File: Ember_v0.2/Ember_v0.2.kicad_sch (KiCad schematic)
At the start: 87 parts, among them J3 DROGUE, J4 BATT_CONN, J5 MAIN, J6 MAN2, J7 DROGUE2, J8 ARM, Q1 SISA96DN-T1, Q2 SISA96DN-T1, Q3 SISA96DN-T1, Q4 SISA96DN-T1, Q5 CJ3400, U1 LDO Regulator 5v, U2 BNO055, U4 BMP280, U6 ADS1220xPW, U7 RPi Pico 2, U8 ADS1220xPW

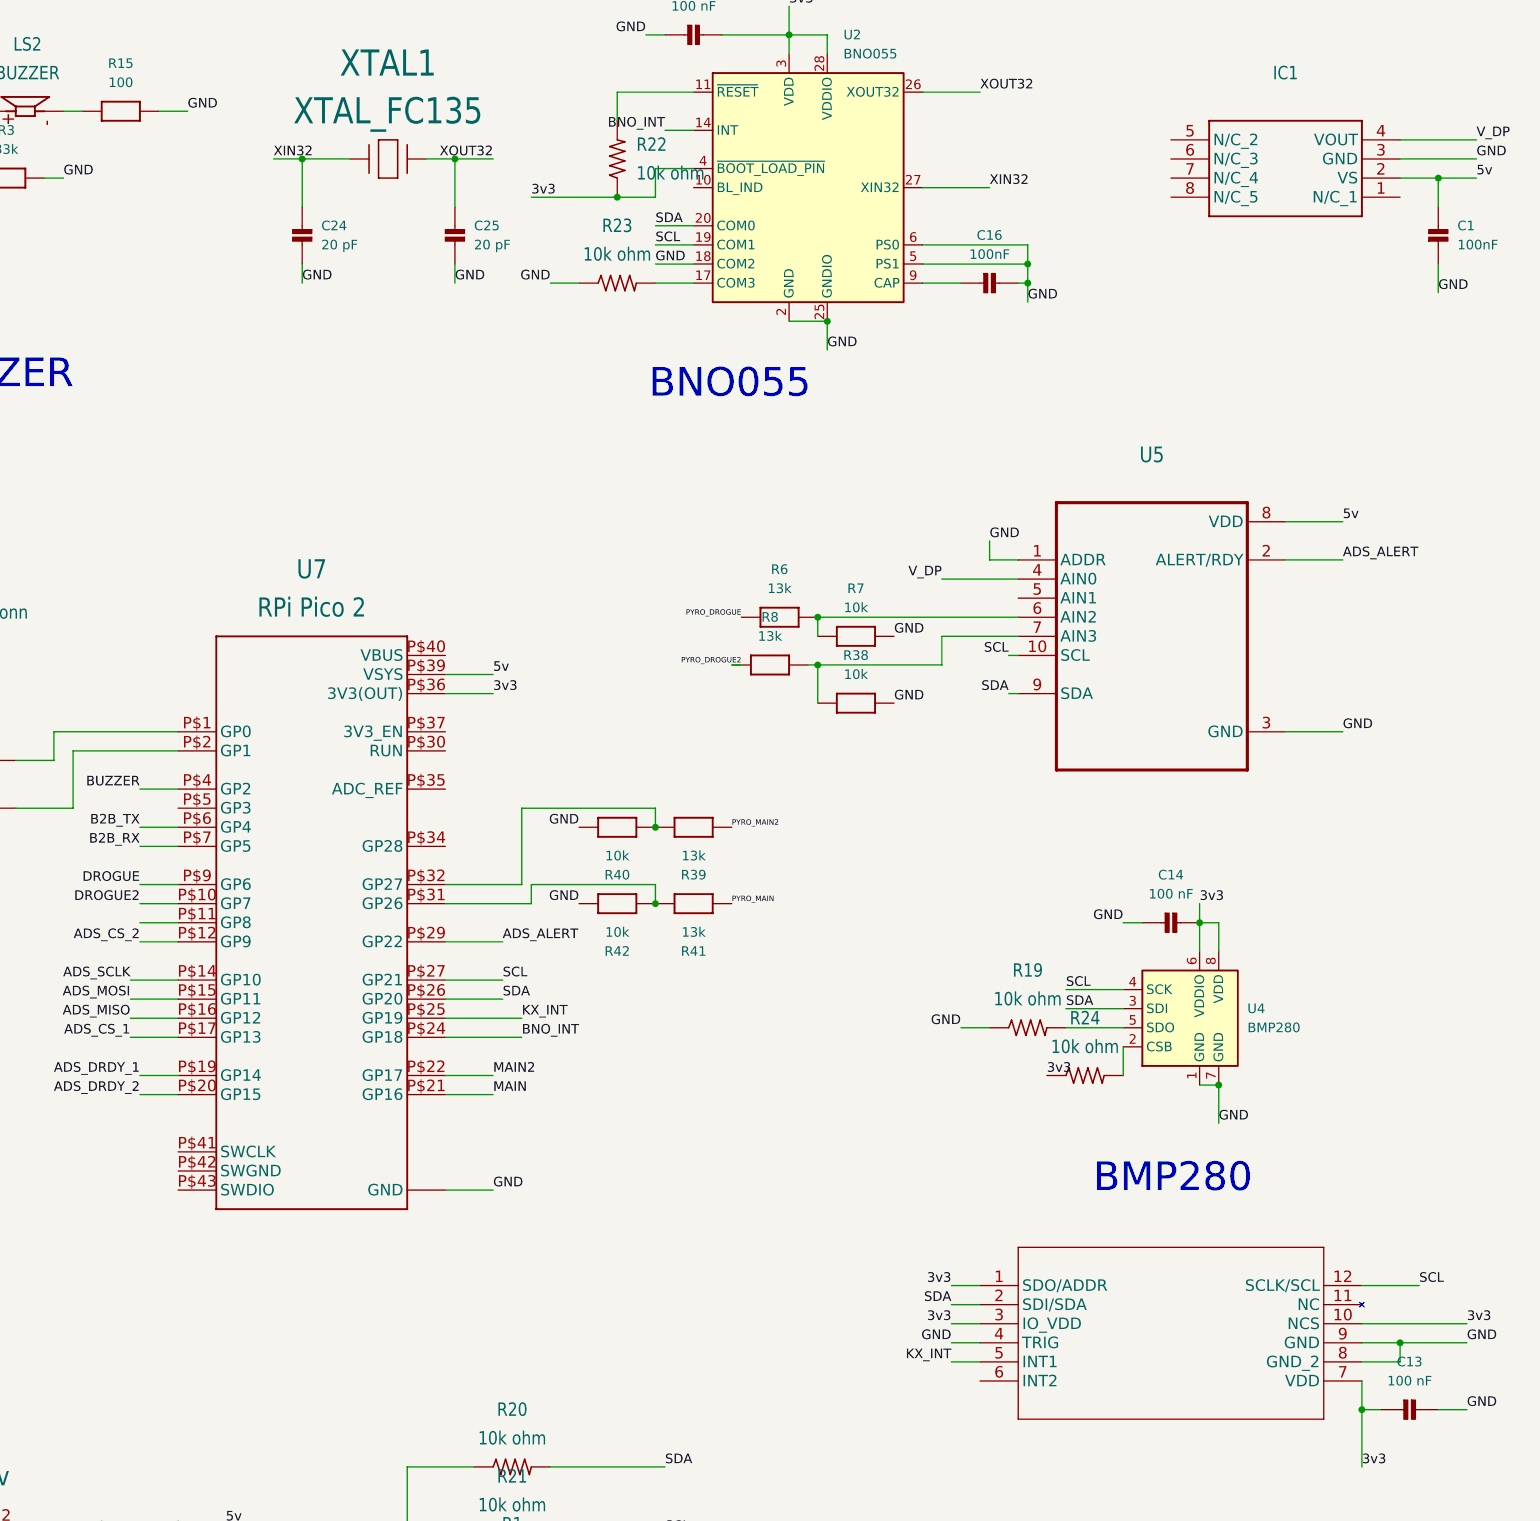
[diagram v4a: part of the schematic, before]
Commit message: main board routing started
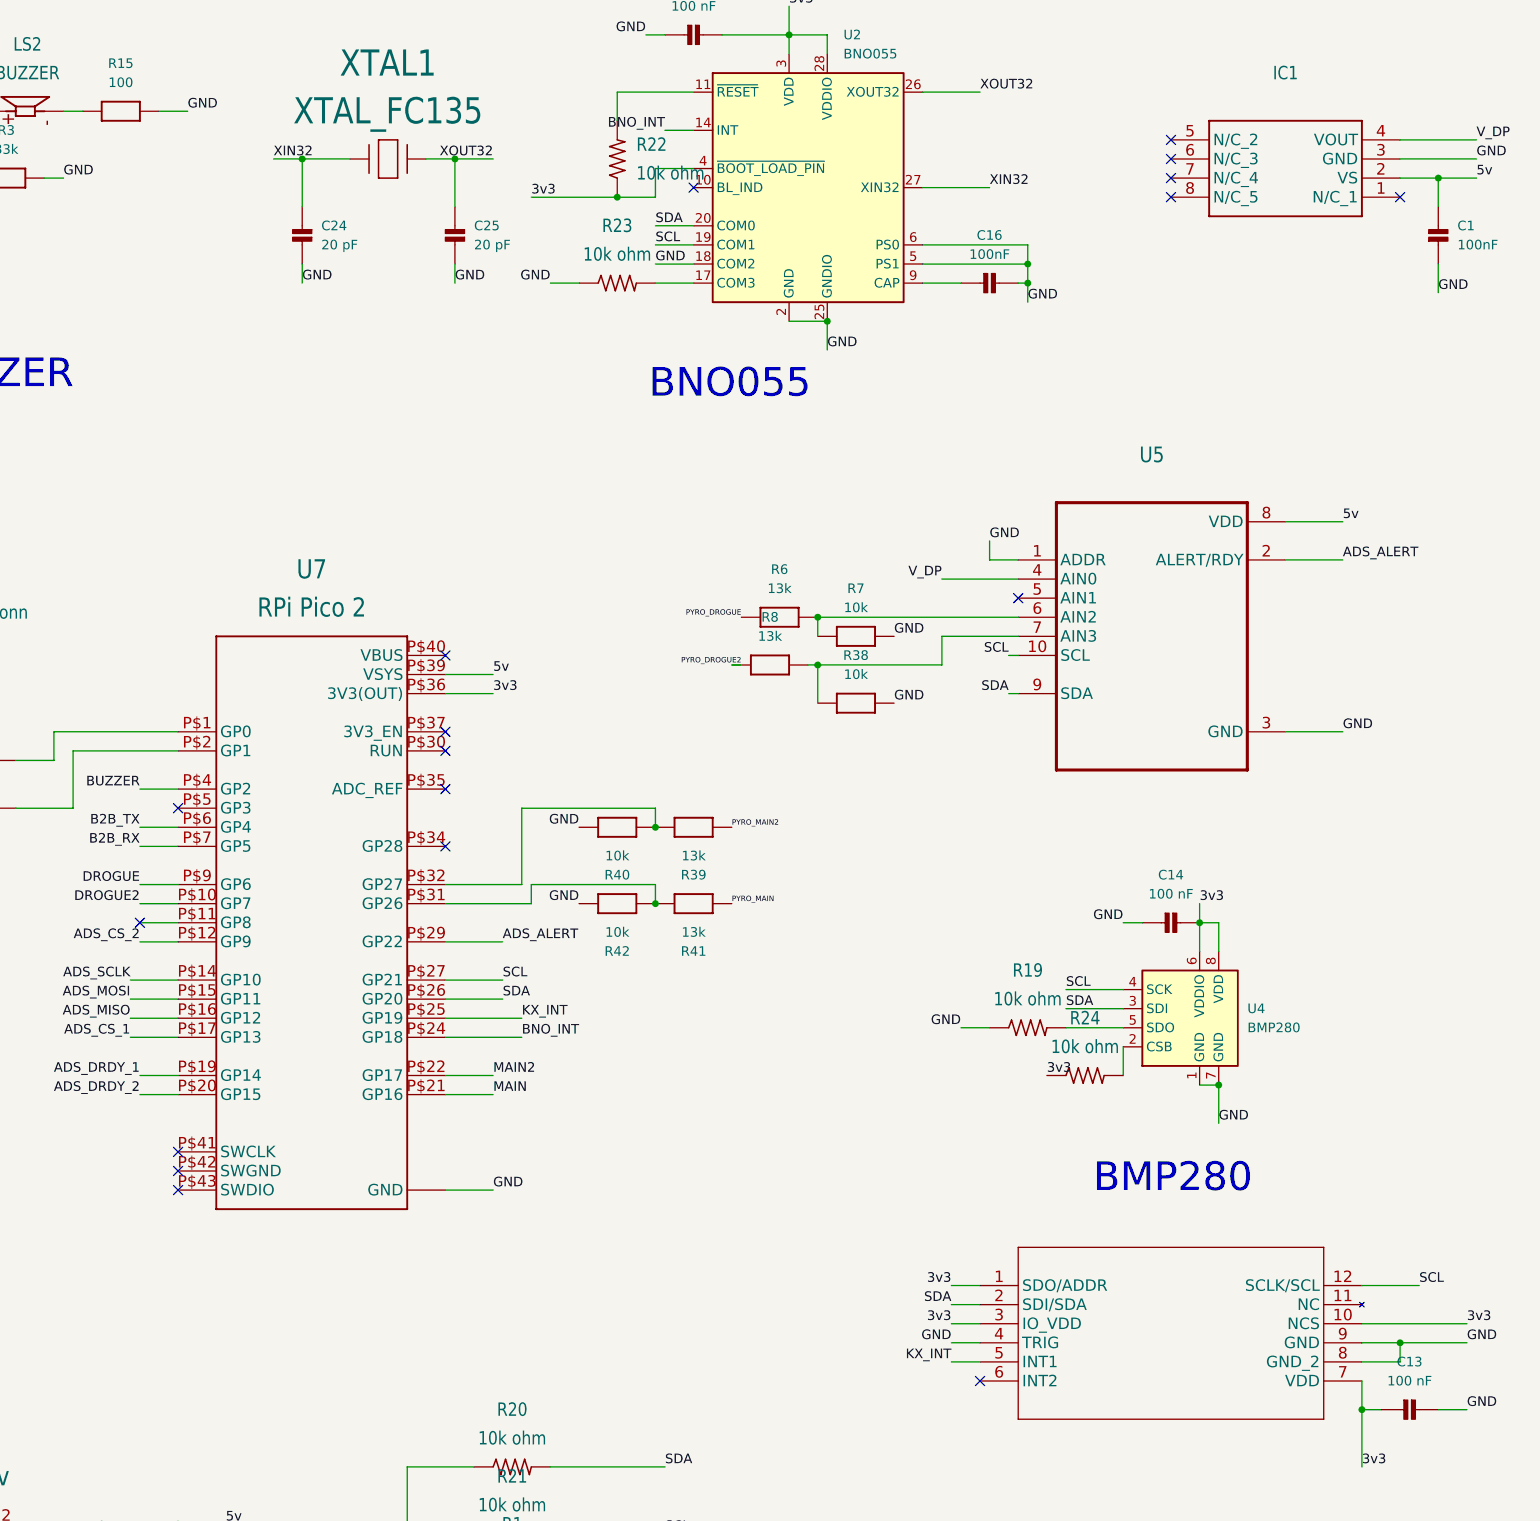
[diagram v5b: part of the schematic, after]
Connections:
- no-connect marks 0 -> 18
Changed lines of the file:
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@@
 		(color 0 0 0 0)
+	)
+	(no_connect
+		(at 384.81 59.69)
+	)
+	(no_connect
+		(at 222.25 186.69)
+	)
+	(no_connect
+		(at 257.81 120.65)
+	)
+	(no_connect
+		(at 217.17 156.21)
+	)
+	(no_connect
+		(at 222.25 191.77)
+	)
+	(no_connect
+		(at 354.33 54.61)
+	)
+	(no_connect
+		(at 334.01 113.03)
+	)
+	(no_connect
+		(at 257.81 138.43)
+	)
+	(no_connect
+		(at 354.33 57.15)
+	)
+	(no_connect
+		(at 290.83 58.42)
+	)
+	(no_connect
+		(at 354.33 59.69)
+	)
+	(no_connect
+		(at 257.81 133.35)
+	)
+	(no_connect
+		(at 354.33 52.07)
+	)
+	(no_connect
+		(at 257.81 146.05)
+	)
+	(no_connect
+		(at 328.93 217.17)
+	)
+	(no_connect
+		(at 257.81 130.81)
+	)
+	(no_connect
+		(at 222.25 189.23)
+	)
+	(no_connect
+		(at 222.25 140.97)
 	)
 	(wire

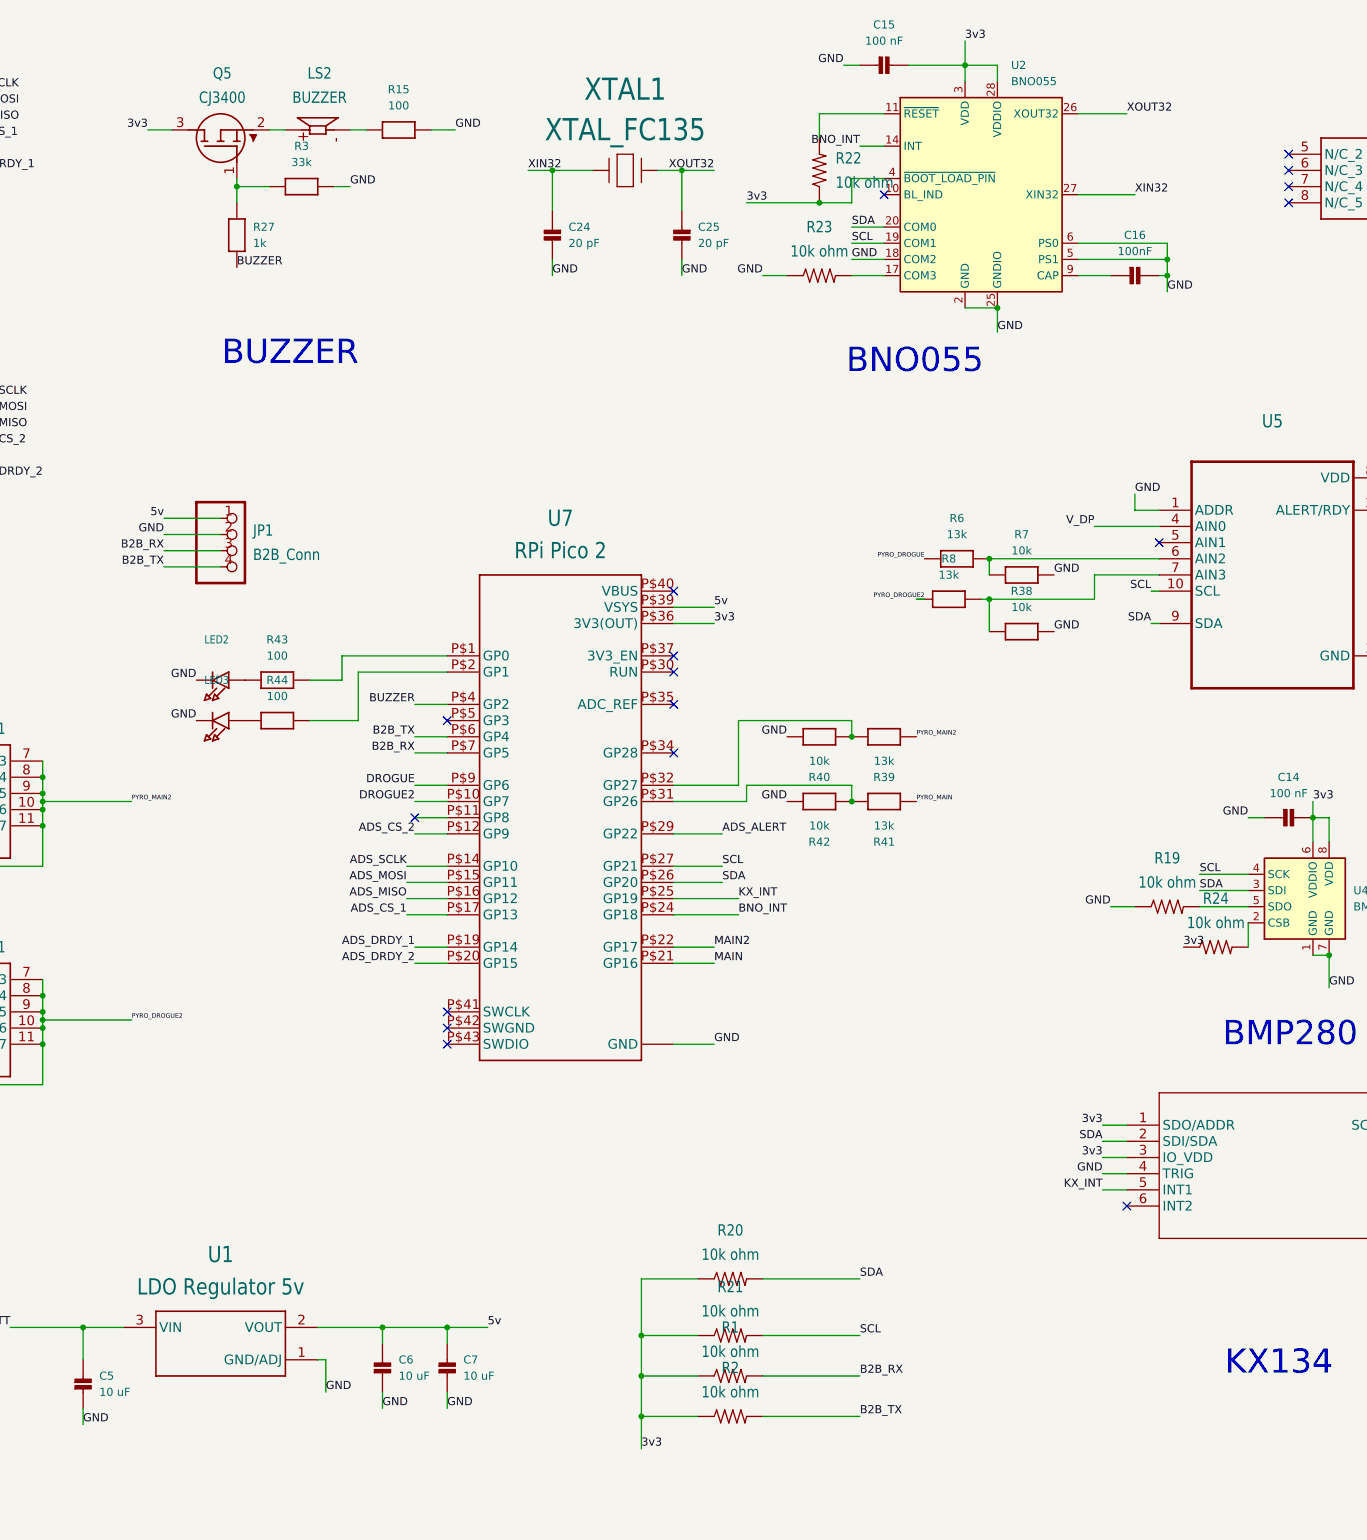
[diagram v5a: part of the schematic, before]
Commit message: Some corrections done and main board routing halfway done
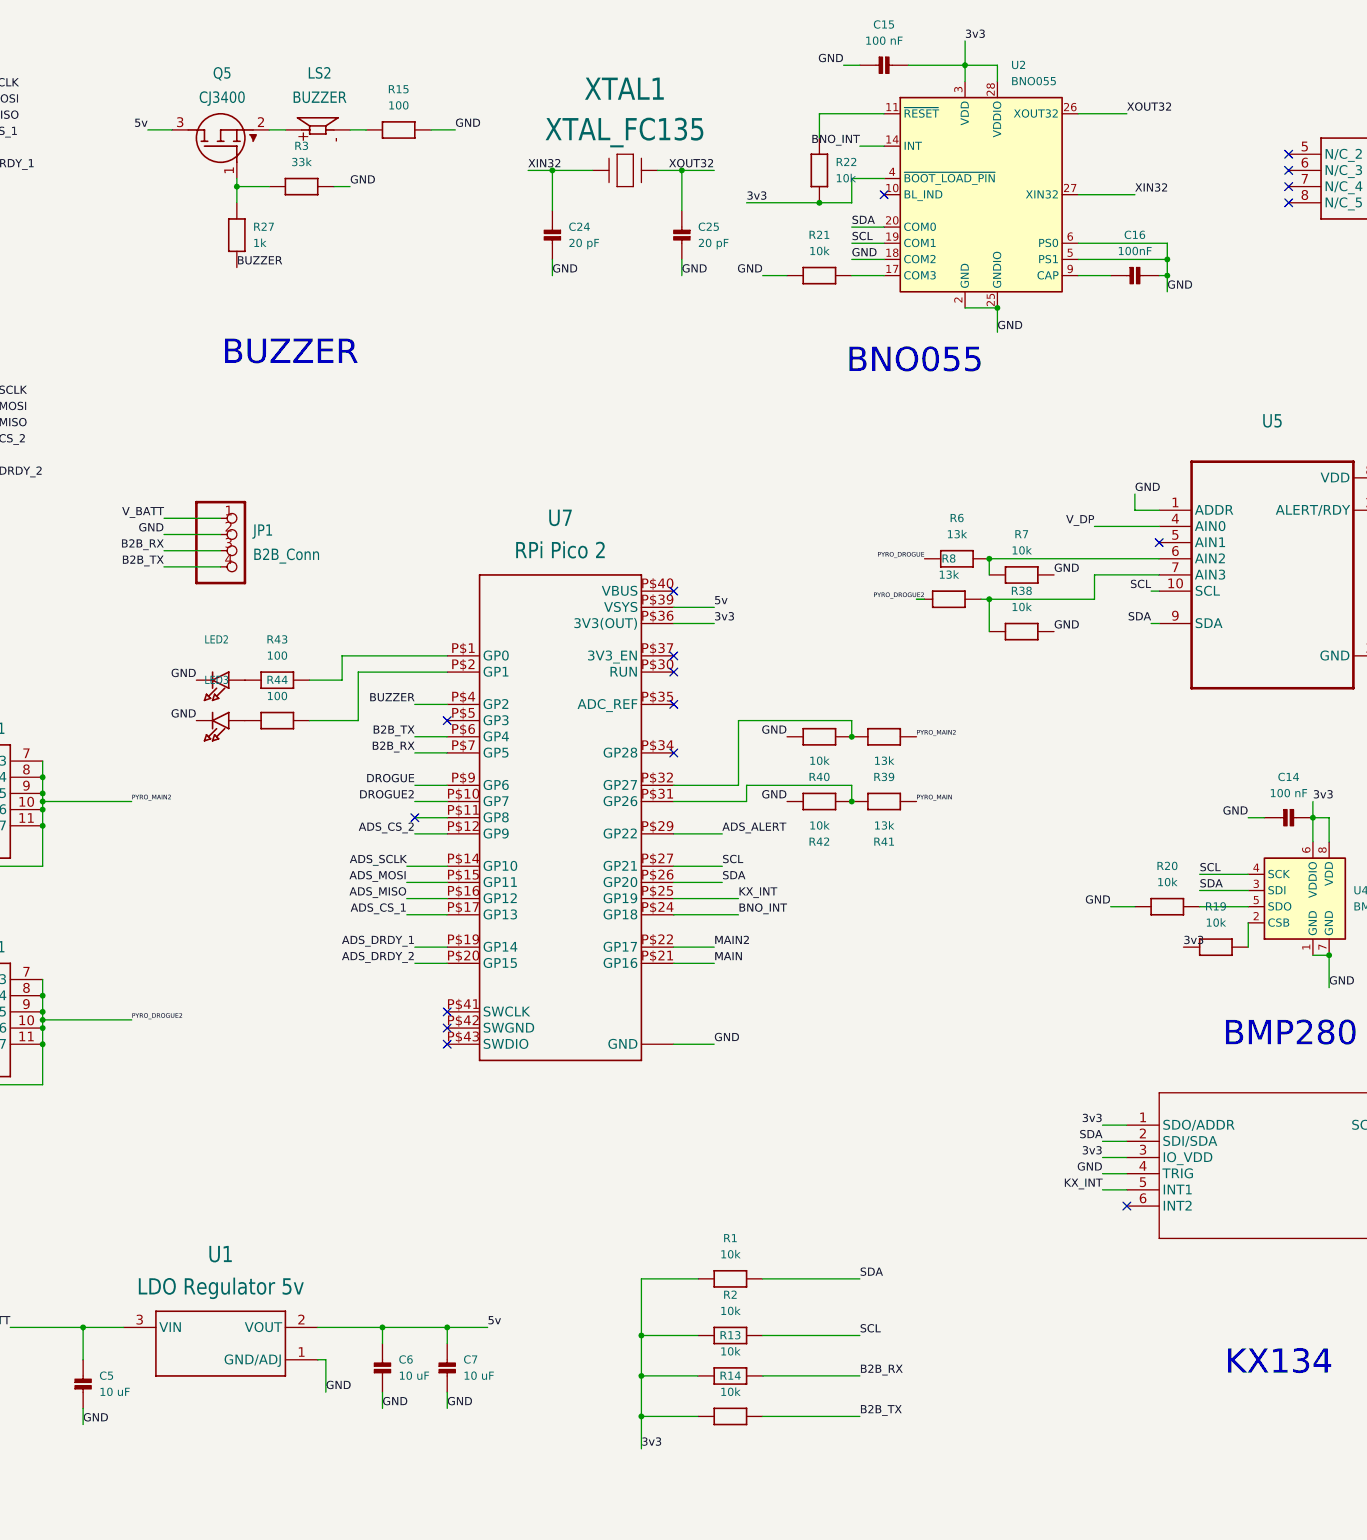
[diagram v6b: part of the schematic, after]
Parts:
- removed R1, R19, R2, R20, R21, R22, R23, R24: 10k ohm, adafruit:R0603, symbol adafruit:R-US_R0603
- added R1, R13, R14, R19, R2, R20, R21, R22: 10k, microbuilder:0603, symbol microbuilder:RESISTOR0603
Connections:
- net 3v3: now also R1.1, R13.1, R14.1, R19.1, R2.1, R22.1; no longer Q5.3 (D)
- net 5v: now also Q5.3 (D); no longer JP1.1
- net B2B_RX: now also R13.2
- net B2B_TX: now also R14.2
- net GND: now also R20.1, R21.1
- net SCL: now also R2.2
- net SDA: now also R1.2
- net V_BATT: now also JP1.1
- net at U4.2 (CSB): now also R19.2
- net at U4.5 (SDO): now also R20.2
- net at U2.11 (~{RESET}): now also R22.2
- net at U2.17 (COM3): now also R21.2
